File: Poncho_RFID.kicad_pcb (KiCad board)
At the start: 2 copper layers, 85.5 x 57 mm, 38 parts, among them U1 CR95HF, Y1 27.12 MHz

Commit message: completado campos kicost
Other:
- net class Default: clearance 0.2 -> 0.25
- rule trace_clearance: 0.2 -> 0.25
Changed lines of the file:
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@@
-(kicad_pcb (version 4) (host pcbnew 4.0.7-e2-6376~58~ubuntu16.04.1)
+(kicad_pcb (version 4) (host pcbnew 4.0.6)
   (general
     (links 108)
     (no_connects 108)
-    (area 0 0 0 0)
+    (area 52.998239 36.09 250.569048 180.435001)
     (thickness 1.6)
     (drawings 4)
@@
   )
   (setup
-    (last_trace_width 0.25)
-    (trace_clearance 0.2)
+    (last_trace_width 1)
+    (user_trace_width 0.4)
+    (user_trace_width 1)
+    (trace_clearance 0.25)
     (zone_clearance 0.508)
     (zone_45_only no)
@@
     (pad_to_mask_clearance 0.2)
     (aux_axis_origin 0 0)
-    (visible_elements FFFFFF7F)
+    (visible_elements 7FFFFFFF)
     (pcbplotparams
       (layerselection 0x00030_80000001)
@@
   (net 76 "Net-(XA1-Pad80)")
   (net_class Default "This is the default net class."
-    (clearance 0.2)
+    (clearance 0.25)
     (trace_width 0.25)
     (via_dia 0.6)

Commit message: PCB definido
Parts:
- moved R5 192.5 mm to (81.3, 146.4), turned to 180 degrees
- moved R8 169.8 mm to (83.1, 133.9), turned to 270 degrees
- moved R7 169.5 mm to (95.4, 133.8), turned to 270 degrees
- moved C1 164.9 mm to (102.4, 153.7)
- moved C7 164.5 mm to (81.3, 139.5), turned to 180 degrees
- moved C8 163.7 mm to (102.3, 146.4), turned to 180 degrees
- moved C10 162.5 mm to (91.8, 127.9), turned to 180 degrees
- moved C19 161.9 mm to (88.8, 116.9)
- moved C9 159.5 mm to (102.3, 142.4), turned to 180 degrees
- moved Y1 158.3 mm to (97.3, 144.4), turned to 90 degrees
- moved R4 154.6 mm to (81.3, 141.9), turned to 180 degrees
- moved C11 150.8 mm to (85.8, 127.9), turned to 180 degrees
- moved C16 150.7 mm to (83.8, 119.9), turned to 270 degrees
- moved C17 149.0 mm to (80.8, 119.9), turned to 270 degrees
- moved R9 147.6 mm to (88.8, 113.9)
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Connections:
- C1 pad 1: Net-(C1-Pad1) -> /VPS_MAIN
- C2 pad 1: Net-(C1-Pad1) -> /VPS_MAIN
- C3 pad 1: Net-(C1-Pad1) -> /VPS_MAIN
- C4 pad 1: Net-(C4-Pad1) -> /VPS_TX
- C5 pad 1: Net-(C4-Pad1) -> /VPS_TX
- C6 pad 1: Net-(C4-Pad1) -> /VPS_TX
- L3 pad 1: Net-(C4-Pad1) -> /VPS_TX
- L3 pad 2: Net-(C1-Pad1) -> /VPS_MAIN
- R1 pad 2: Net-(C1-Pad1) -> /VPS_MAIN
- R3 pad 1: +3V3 -> /VPS_MAIN
- R6 pad 1: +3V3 -> /VPS_MAIN
- U1 pad 13: Net-(U1-Pad13) -> /VPS_MAIN
- U1 pad 32: Net-(U1-Pad32) -> /VPS_TX
- XA1 pad 41: +3V3 -> Net-(XA1-Pad41)
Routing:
- net Net-(AE1-Pad1): track 0.00 -> 594.8 mm, vias 0 -> 4
- net /VPS_MAIN: track 0.00 -> 53.3 mm, vias 0 -> 2
- net /MOSI: track 0.00 -> 46.5 mm
- net Net-(U1-Pad18): track 0.00 -> 46.5 mm, vias 0 -> 2
- net Net-(U1-Pad16): track 0.00 -> 42.3 mm, vias 0 -> 1
- net +3V3: track 0.00 -> 42.0 mm
- net Net-(AE1-Pad2): track 0.00 -> 32.6 mm
- net /CS: track 0.00 -> 28.1 mm
- net Net-(C11-Pad2): track 0.00 -> 15.6 mm
- net Net-(C10-Pad1): track 0.00 -> 14.8 mm
- net Net-(C8-Pad2): track 0.00 -> 12.6 mm
- net /VPS_TX: track 0.00 -> 11.4 mm
- net GND: track 0.00 -> 10.7 mm, vias 0 -> 140
- net Net-(R7-Pad2): track 0.00 -> 10.2 mm, vias 0 -> 2
- net Net-(R5-Pad1): track 0.00 -> 9.99 mm, vias 0 -> 2
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- added copper zone on B.Cu, net GND
- added copper zone on F.Cu, net GND
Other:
- board size 85.5 x 57 mm -> 85.5 x 90.8 mm
- net class Default: clearance 0.25 -> 0.2
- rule trace_clearance: 0.25 -> 0.2

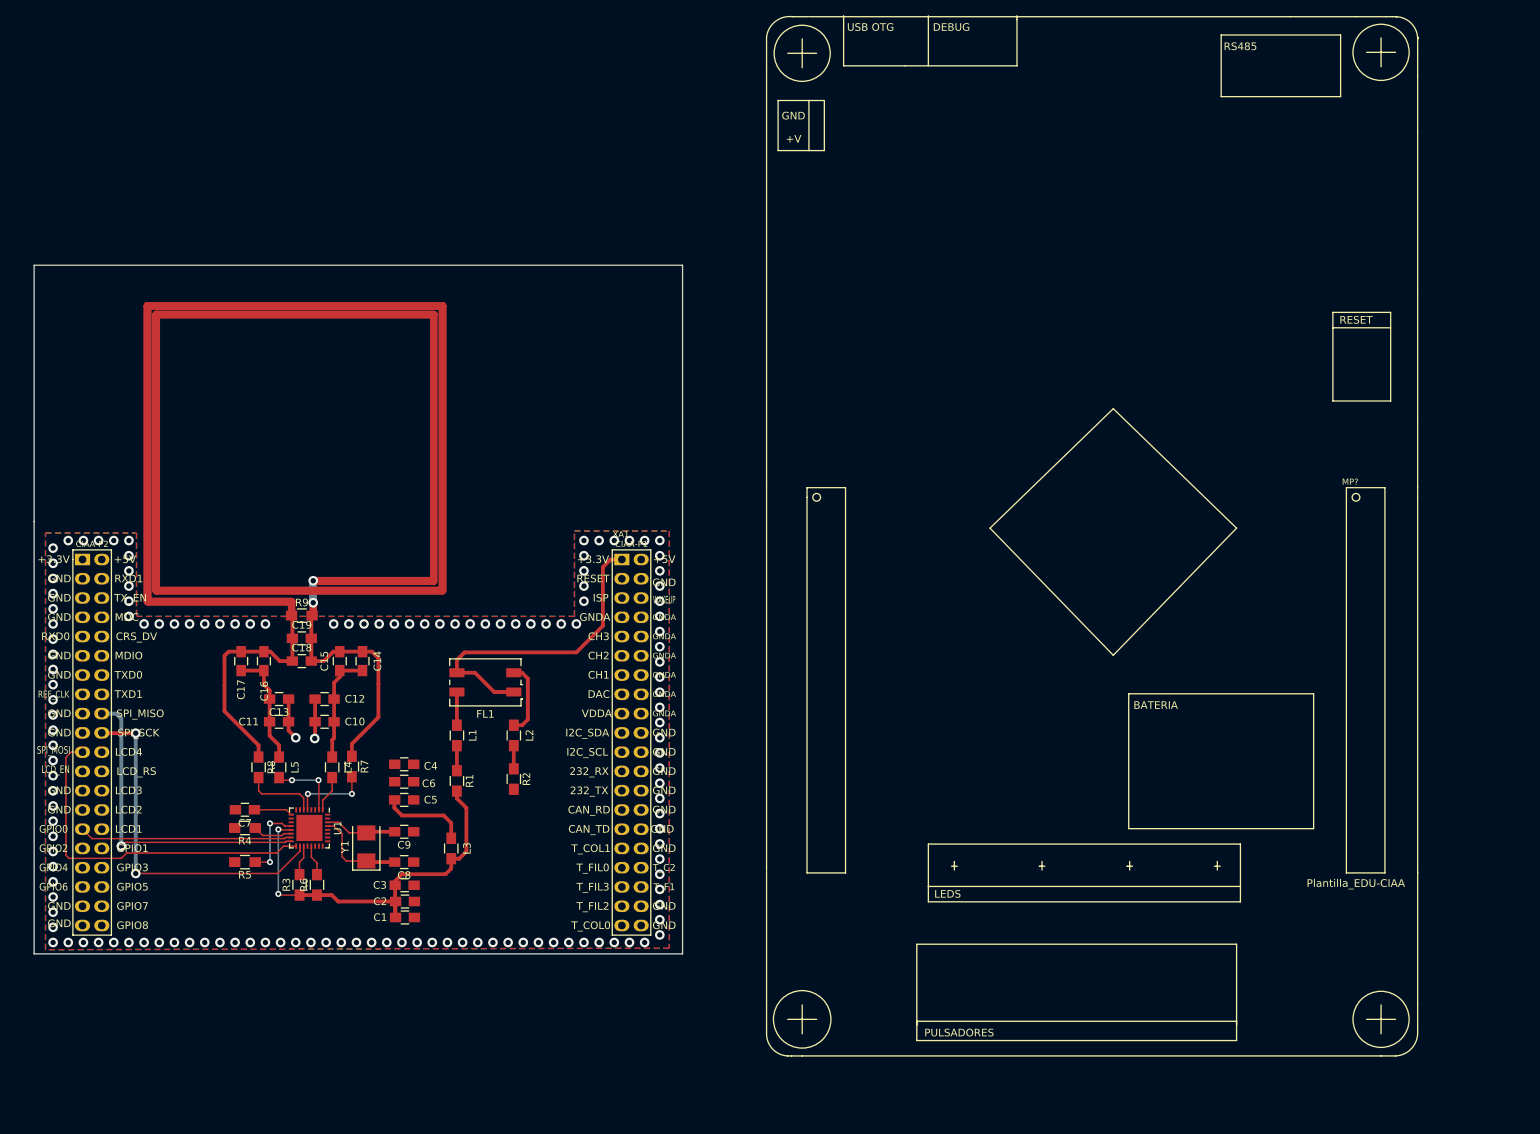
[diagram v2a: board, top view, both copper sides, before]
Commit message: Serigrafia ordenada
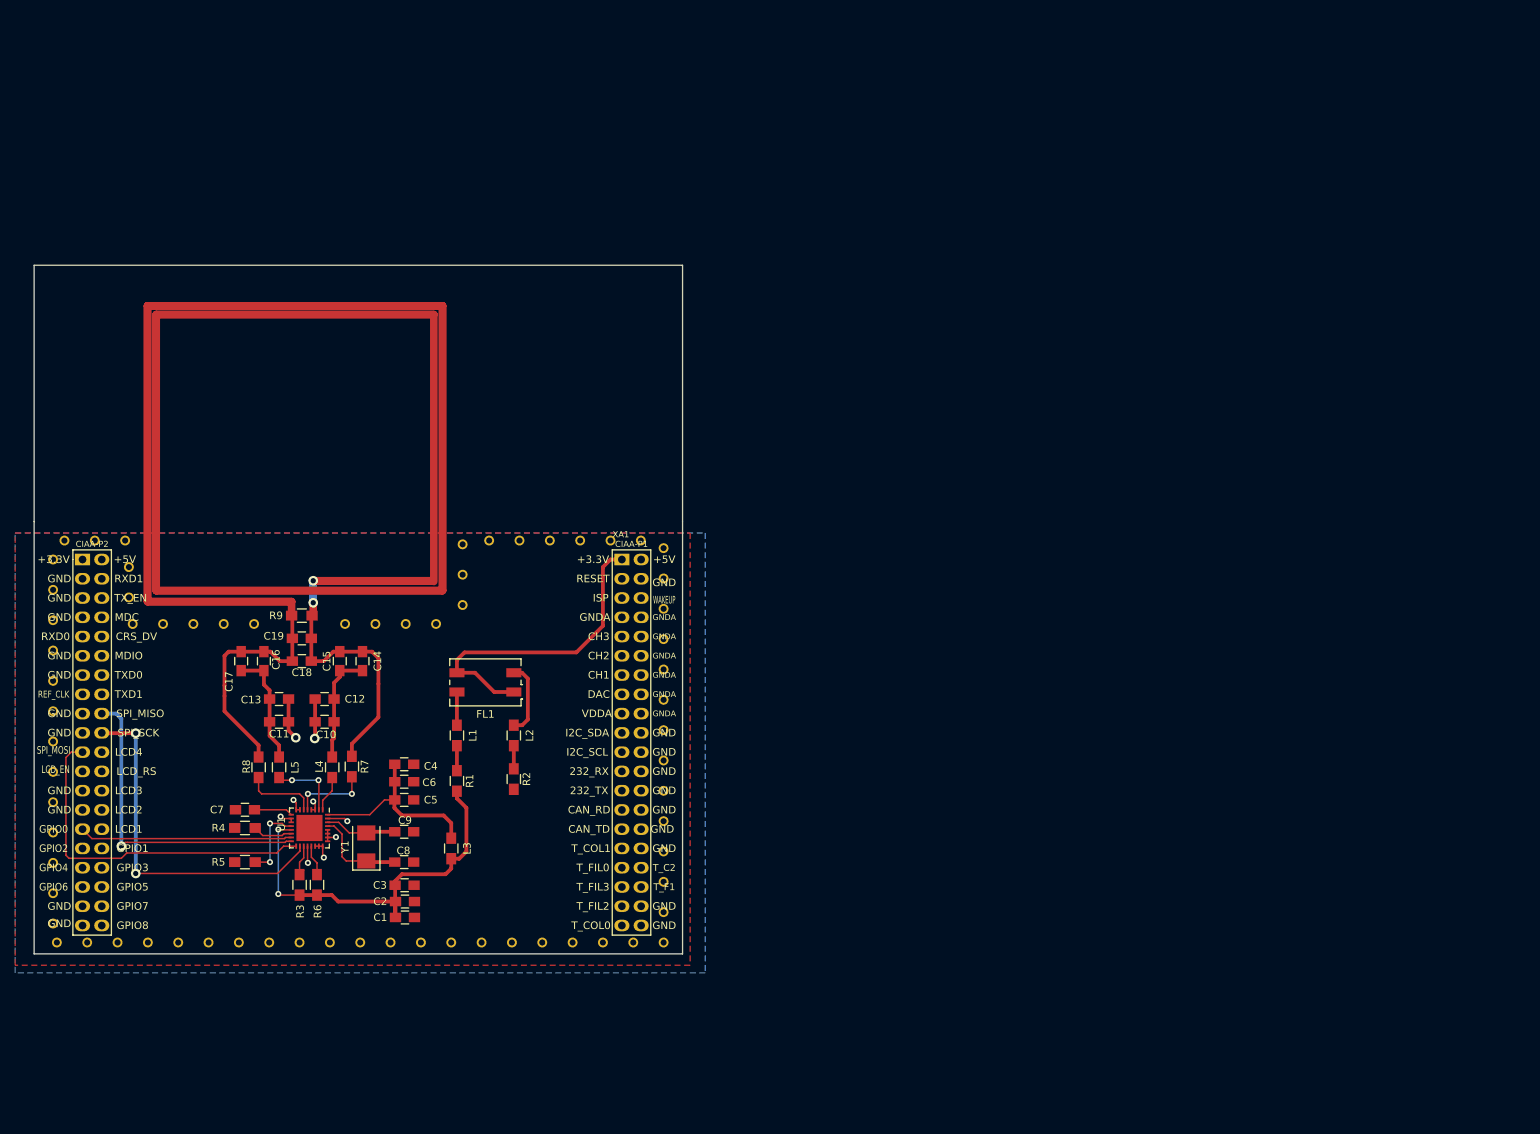
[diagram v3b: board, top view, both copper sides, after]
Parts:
- removed MP?: Plantilla_EDU-CIAA, poncho_RFID:Plantilla_EDU-CIAA
- added REF**: via_stich, poncho_RFID:via_stich, F.Cu at (110.0, 104.5)
- added REF**: via_stich, poncho_RFID:via_stich, F.Cu at (56.0, 146.5)
- added REF**: via_stich, poncho_RFID:via_stich, F.Cu at (56.0, 142.5)
- added REF**: via_stich, poncho_RFID:via_stich, F.Cu at (56.0, 138.5)
- added REF**: via_stich, poncho_RFID:via_stich, F.Cu at (56.0, 134.5)
- added REF**: via_stich, poncho_RFID:via_stich, F.Cu at (56.0, 130.5)
- added REF**: via_stich, poncho_RFID:via_stich, F.Cu at (56.0, 126.5)
- added REF**: via_stich, poncho_RFID:via_stich, F.Cu at (56.0, 122.5)
- added REF**: via_stich, poncho_RFID:via_stich, F.Cu at (56.0, 118.5)
- added REF**: via_stich, poncho_RFID:via_stich, F.Cu at (56.0, 114.5)
- added REF**: via_stich, poncho_RFID:via_stich, F.Cu at (56.0, 110.5)
- added REF**: via_stich, poncho_RFID:via_stich, F.Cu at (113.5, 104.0)
- added REF**: via_stich, poncho_RFID:via_stich, F.Cu at (56.0, 106.5)
- added REF**: via_stich, poncho_RFID:via_stich, F.Cu at (57.5, 104.0)
- added REF**: via_stich, poncho_RFID:via_stich, F.Cu at (61.5, 104.0)
- added REF**: via_stich, poncho_RFID:via_stich, F.Cu at (65.5, 104.0)
- added REF**: via_stich, poncho_RFID:via_stich, F.Cu at (66.0, 107.5)
- added REF**: via_stich, poncho_RFID:via_stich, F.Cu at (66.0, 111.5)
- added REF**: via_stich, poncho_RFID:via_stich, F.Cu at (66.5, 115.0)
- added REF**: via_stich, poncho_RFID:via_stich, F.Cu at (70.5, 115.0)
- added REF**: via_stich, poncho_RFID:via_stich, F.Cu at (74.5, 115.0)
- added REF**: via_stich, poncho_RFID:via_stich, F.Cu at (78.5, 115.0)
- added REF**: via_stich, poncho_RFID:via_stich, F.Cu at (117.5, 104.0)
- added REF**: via_stich, poncho_RFID:via_stich, F.Cu at (82.5, 115.0)
- added REF**: via_stich, poncho_RFID:via_stich, F.Cu at (94.5, 115.0)
- added REF**: via_stich, poncho_RFID:via_stich, F.Cu at (98.5, 115.0)
- added REF**: via_stich, poncho_RFID:via_stich, F.Cu at (102.5, 115.0)
- added REF**: via_stich, poncho_RFID:via_stich, F.Cu at (106.5, 115.0)
- added REF**: via_stich, poncho_RFID:via_stich, F.Cu at (110.0, 112.5)
- added REF**: via_stich, poncho_RFID:via_stich, F.Cu at (110.0, 108.5)
- added REF**: via_stich, poncho_RFID:via_stich, F.Cu at (136.5, 105.0)
- added REF**: via_stich, poncho_RFID:via_stich, F.Cu at (136.5, 109.0)
- added REF**: via_stich, poncho_RFID:via_stich, F.Cu at (136.5, 113.0)
- added REF**: via_stich, poncho_RFID:via_stich, F.Cu at (121.5, 104.0)
- added REF**: via_stich, poncho_RFID:via_stich, F.Cu at (136.5, 117.0)
- added REF**: via_stich, poncho_RFID:via_stich, F.Cu at (136.5, 121.0)
- added REF**: via_stich, poncho_RFID:via_stich, F.Cu at (136.5, 125.0)
- added REF**: via_stich, poncho_RFID:via_stich, F.Cu at (136.5, 129.0)
- added REF**: via_stich, poncho_RFID:via_stich, F.Cu at (136.5, 133.0)
- added REF**: via_stich, poncho_RFID:via_stich, F.Cu at (136.5, 137.0)
- added REF**: via_stich, poncho_RFID:via_stich, F.Cu at (136.5, 141.0)
- added REF**: via_stich, poncho_RFID:via_stich, F.Cu at (136.5, 145.0)
- added REF**: via_stich, poncho_RFID:via_stich, F.Cu at (136.5, 149.0)
- added REF**: via_stich, poncho_RFID:via_stich, F.Cu at (136.5, 153.0)
- added REF**: via_stich, poncho_RFID:via_stich, F.Cu at (125.5, 104.0)
- added REF**: via_stich, poncho_RFID:via_stich, F.Cu at (136.5, 157.0)
- added REF**: via_stich, poncho_RFID:via_stich, F.Cu at (132.5, 157.0)
- added REF**: via_stich, poncho_RFID:via_stich, F.Cu at (128.5, 157.0)
- added REF**: via_stich, poncho_RFID:via_stich, F.Cu at (124.5, 157.0)
- added REF**: via_stich, poncho_RFID:via_stich, F.Cu at (120.5, 157.0)
- added REF**: via_stich, poncho_RFID:via_stich, F.Cu at (116.5, 157.0)
- added REF**: via_stich, poncho_RFID:via_stich, F.Cu at (112.5, 157.0)
- added REF**: via_stich, poncho_RFID:via_stich, F.Cu at (108.5, 157.0)
- added REF**: via_stich, poncho_RFID:via_stich, F.Cu at (104.5, 157.0)
- added REF**: via_stich, poncho_RFID:via_stich, F.Cu at (100.5, 157.0)
- added REF**: via_stich, poncho_RFID:via_stich, F.Cu at (129.5, 104.0)
- added REF**: via_stich, poncho_RFID:via_stich, F.Cu at (96.5, 157.0)
- added REF**: via_stich, poncho_RFID:via_stich, F.Cu at (92.5, 157.0)
- added REF**: via_stich, poncho_RFID:via_stich, F.Cu at (88.5, 157.0)
- added REF**: via_stich, poncho_RFID:via_stich, F.Cu at (84.5, 157.0)
- added REF**: via_stich, poncho_RFID:via_stich, F.Cu at (80.5, 157.0)
- added REF**: via_stich, poncho_RFID:via_stich, F.Cu at (76.5, 157.0)
- added REF**: via_stich, poncho_RFID:via_stich, F.Cu at (72.5, 157.0)
- added REF**: via_stich, poncho_RFID:via_stich, F.Cu at (68.5, 157.0)
- added REF**: via_stich, poncho_RFID:via_stich, F.Cu at (64.5, 157.0)
- added REF**: via_stich, poncho_RFID:via_stich, F.Cu at (60.5, 157.0)
- added REF**: via_stich, poncho_RFID:via_stich, F.Cu at (133.5, 104.0)
- added REF**: via_stich, poncho_RFID:via_stich, F.Cu at (56.5, 157.0)
- added REF**: via_stich, poncho_RFID:via_stich, F.Cu at (56.0, 154.5)
- added REF**: via_stich, poncho_RFID:via_stich, F.Cu at (56.0, 150.5)
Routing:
- net GND: track 10.7 -> 26.7 mm, vias 140 -> 9
- net /VPS_TX: track 11.4 -> 25.8 mm

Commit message: Ultimas correcciones
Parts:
- added G***: LOGO, poncho_RFID:Logo_Poncho, F.Cu at (124.0, 78.0)
- added G101: Logo_OSHWA, poncho_RFID:Logo_OSHWA, F.Cu at (124.0, 90.0)
- added REF**: 1pin, Connectors:1pin, F.Cu at (59.0, 73.0)
- added REF**: 1pin, Connectors:1pin, F.Cu at (134.0, 73.0)
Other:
- board text added: "Diametro minimo de agujero: 0,4 mm Diametro minimo de pad o via: 0,8 mm Ancho minimo de traza: 0,20 mm Separacion minima entre trazas: 0,20mm Capas: 2 Terminacion superficial: HASL"
- board text added: "Industria Argentina"
